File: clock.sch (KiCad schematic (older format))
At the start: 14 parts, among them J1 C:PAL / O:NTSC, U16 74LS14, U28 8701, U29 7406, Y2 17.73447 MHz (PAL) / 14.31818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

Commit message: Fix R47/R101
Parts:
- added R47: 1k, Open128:R_Axial_DIN0309_L9.0mm_D2.5mm_P12.70mm_Horizontal, symbol Device:R
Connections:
- net +5V: now also R47.1
- net at FB18.2, U29.2: now also R47.2
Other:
- moved on the sheet: FB18
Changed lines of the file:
@@
 Wire Wire Line
 	2550 2950 2550 3000
-Text HLabel 5550 2050 2    50   Output ~ 0
+Text HLabel 6600 2050 2    50   Output ~ 0
 ϕCOLOR
 Wire Wire Line
-	3900 2050 5550 2050
-Text HLabel 5550 1950 2    50   Output ~ 0
+	3900 2050 6600 2050
+Text HLabel 6600 1950 2    50   Output ~ 0
 ϕDOT
 Wire Wire Line
@@
 	4100 1750 4250 1750
 Wire Wire Line
-	4100 1950 5550 1950
+	4100 1950 6600 1950
 $Comp
 L 74xx:74LS06 U29
@@
 	1    0    0    -1
 $EndComp
-Text HLabel 5550 1750 2    50   Output ~ 0
+Text HLabel 6600 1750 2    50   Output ~ 0
 ~ϕDOT
 Wire Wire Line
-	5550 1750 5250 1750
+	6600 1750 6300 1750
 Connection ~ 4100 1950
 $Comp
 L Open128:Ferrite_Bead FB18
 U 1 1 5DC5C94F
-P 5150 1750
-F 0 "FB18" V 5005 1750 50  0000 C CNN
-F 1 "Ferrite_Bead_Small" V 5004 1750 50  0001 C CNN
-F 2 "Open128:Ferrite_Bead_vertical" V 5080 1750 50  0001 C CNN
-F 3 "~" H 5150 1750 50  0001 C CNN
-F 4 "81-BL02RN2R1M2B" H 5150 1750 50  0001 C CNN "Mouser Part"
-	1    5150 1750
+P 6200 1750
+F 0 "FB18" V 6055 1750 50  0000 C CNN
+F 1 "Ferrite_Bead_Small" V 6054 1750 50  0001 C CNN
+F 2 "Open128:Ferrite_Bead_vertical" V 6130 1750 50  0001 C CNN
+F 3 "~" H 6200 1750 50  0001 C CNN
+F 4 "81-BL02RN2R1M2B" H 6200 1750 50  0001 C CNN "Mouser Part"
+	1    6200 1750
 	0    1    1    0
 $EndComp
 Wire Wire Line
-	5050 1750 4850 1750
+	6100 1750 5400 1750
 $Comp
 L power:PWR_FLAG #FLG0101
@@
 	3500 2850 3400 2850
 Connection ~ 3400 2850
+$Comp
+L Device:R R47
+U 1 1 60D4A27C
+P 5400 1450
+F 0 "R47" H 5470 1496 50  0000 L CNN
+F 1 "1k" V 5400 1400 50  0000 L CNN
+F 2 "Open128:R_Axial_DIN0309_L9.0mm_D2.5mm_P12.70mm_Horizontal" V 5330 1450 50  0001 C CNN
+F 3 "~" H 5400 1450 50  0001 C CNN
+F 4 "660-MF1/4DCT52R5600F" H 5400 1450 50  0001 C CNN "Mouser Part"
+	1    5400 1450
+	1    0    0    -1
+$EndComp
+$Comp
+L power:+5V #PWR?
+U 1 1 60D4B17E
+P 5400 1200
+F 0 "#PWR?" H 5400 1050 50  0001 C CNN
+F 1 "+5V" H 5415 1373 50  0000 C CNN
+F 2 "" H 5400 1200 50  0001 C CNN
+F 3 "" H 5400 1200 50  0001 C CNN
+	1    5400 1200
+	1    0    0    -1
+$EndComp
+Wire Wire Line
+	5400 1200 5400 1300
+Wire Wire Line
+	5400 1600 5400 1750
+Connection ~ 5400 1750
+Wire Wire Line
+	5400 1750 4850 1750
 $EndSCHEMATC

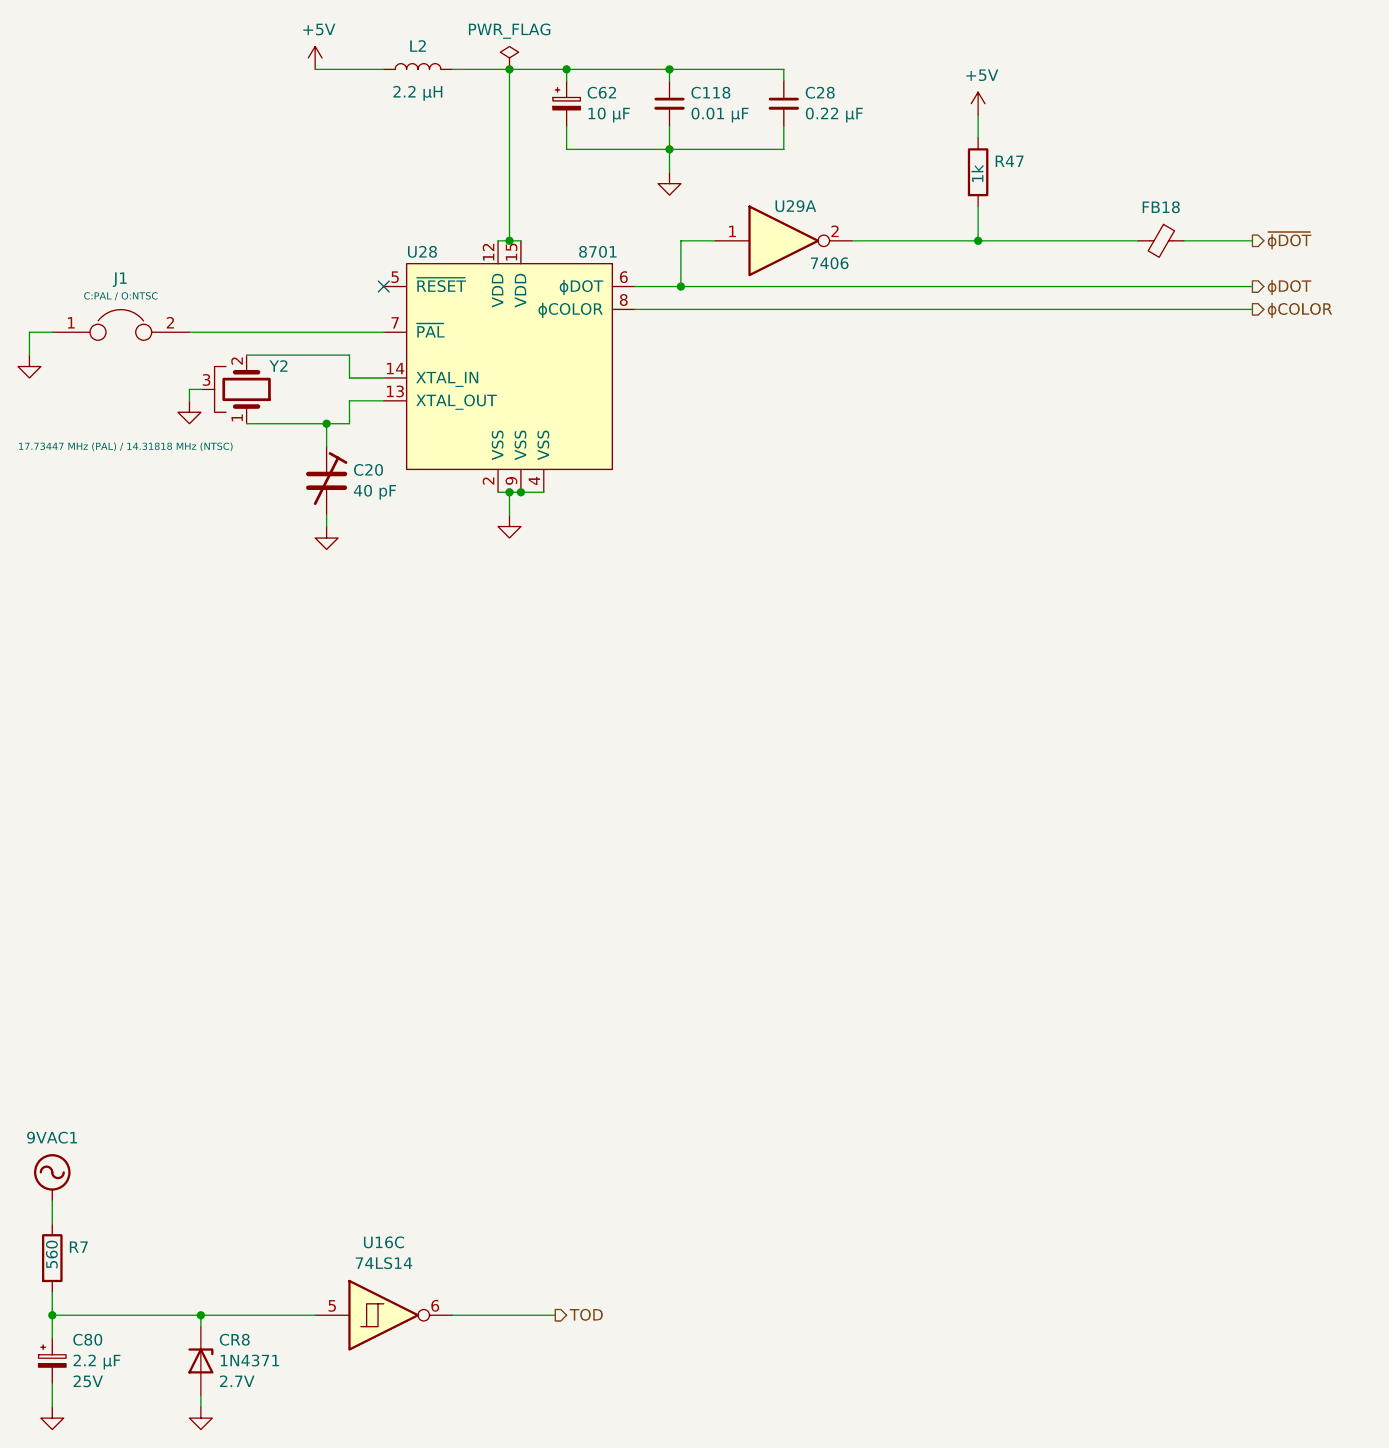
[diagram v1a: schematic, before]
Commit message: Clean up schematic
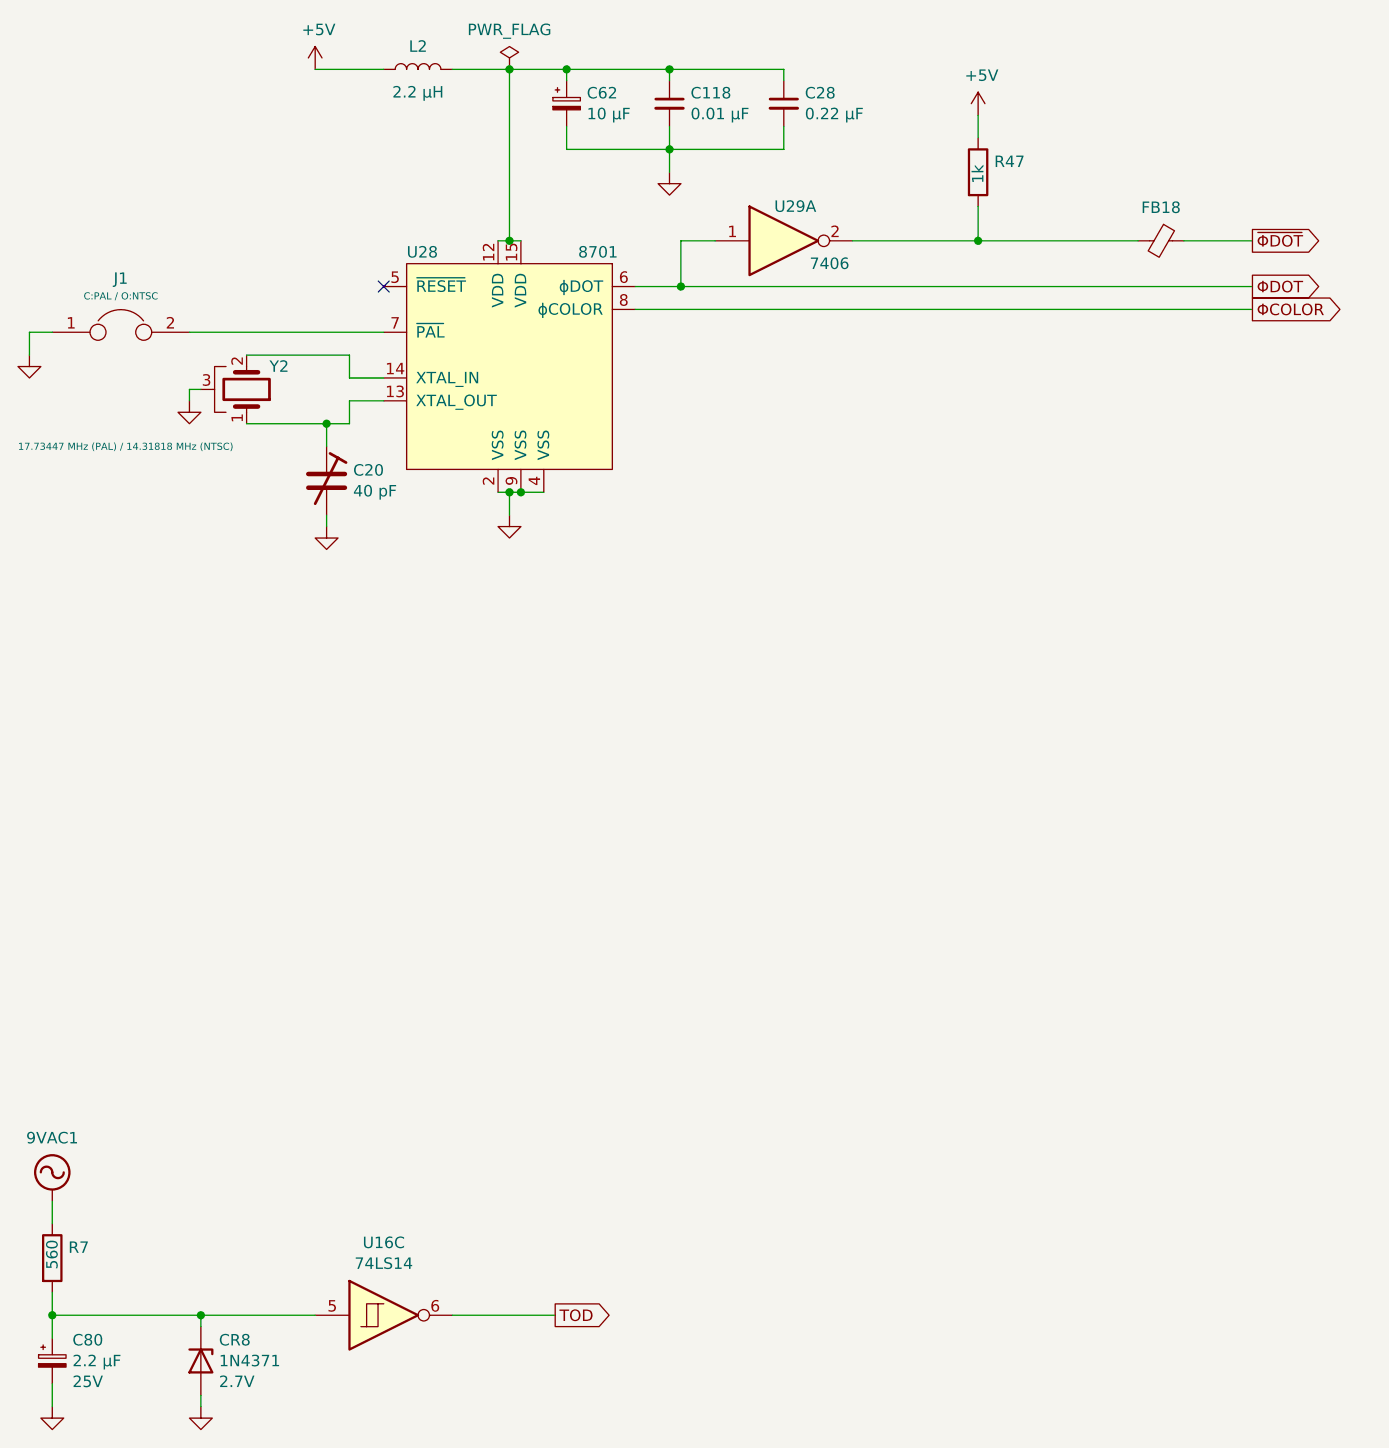
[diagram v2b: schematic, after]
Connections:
- net ~ϕDOT renamed ~ΦDOT
- net ϕCOLOR renamed ΦCOLOR
- net ϕDOT renamed ΦDOT
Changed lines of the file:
@@
 Wire Wire Line
 	3100 6450 3550 6450
-Text HLabel 3550 6450 2    50   Output ~ 0
-TOD
 Wire Wire Line
 	3300 2850 3350 2850
@@
 Wire Wire Line
 	2550 2950 2550 3000
-Text HLabel 6600 2050 2    50   Output ~ 0
-ϕCOLOR
 Wire Wire Line
 	3900 2050 6600 2050
-Text HLabel 6600 1950 2    50   Output ~ 0
-ϕDOT
 Wire Wire Line
 	3900 1950 4100 1950
@@
 	1    0    0    -1
 $EndComp
-Text HLabel 6600 1750 2    50   Output ~ 0
-~ϕDOT
 Wire Wire Line
 	6600 1750 6300 1750
@@
 $EndComp
 $Comp
-L power:+5V #PWR?
+L power:+5V #PWR0448
 U 1 1 60D4B17E
 P 5400 1200
-F 0 "#PWR?" H 5400 1050 50  0001 C CNN
+F 0 "#PWR0448" H 5400 1050 50  0001 C CNN
 F 1 "+5V" H 5415 1373 50  0000 C CNN
 F 2 "" H 5400 1200 50  0001 C CNN
@@
 Wire Wire Line
 	5400 1750 4850 1750
+Text GLabel 3550 6450 2    50   Output ~ 0
+TOD
+Text GLabel 6600 1750 2    50   Output ~ 0
+~ΦDOT
+Text GLabel 6600 1950 2    50   Output ~ 0
+ΦDOT
+Text GLabel 6600 2050 2    50   Output ~ 0
+ΦCOLOR
 $EndSCHEMATC
